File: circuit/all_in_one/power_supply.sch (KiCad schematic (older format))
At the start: 23 parts, among them Q1 2SB647, Q2 2SK2611, U1 LM7805, U2 MC34063A

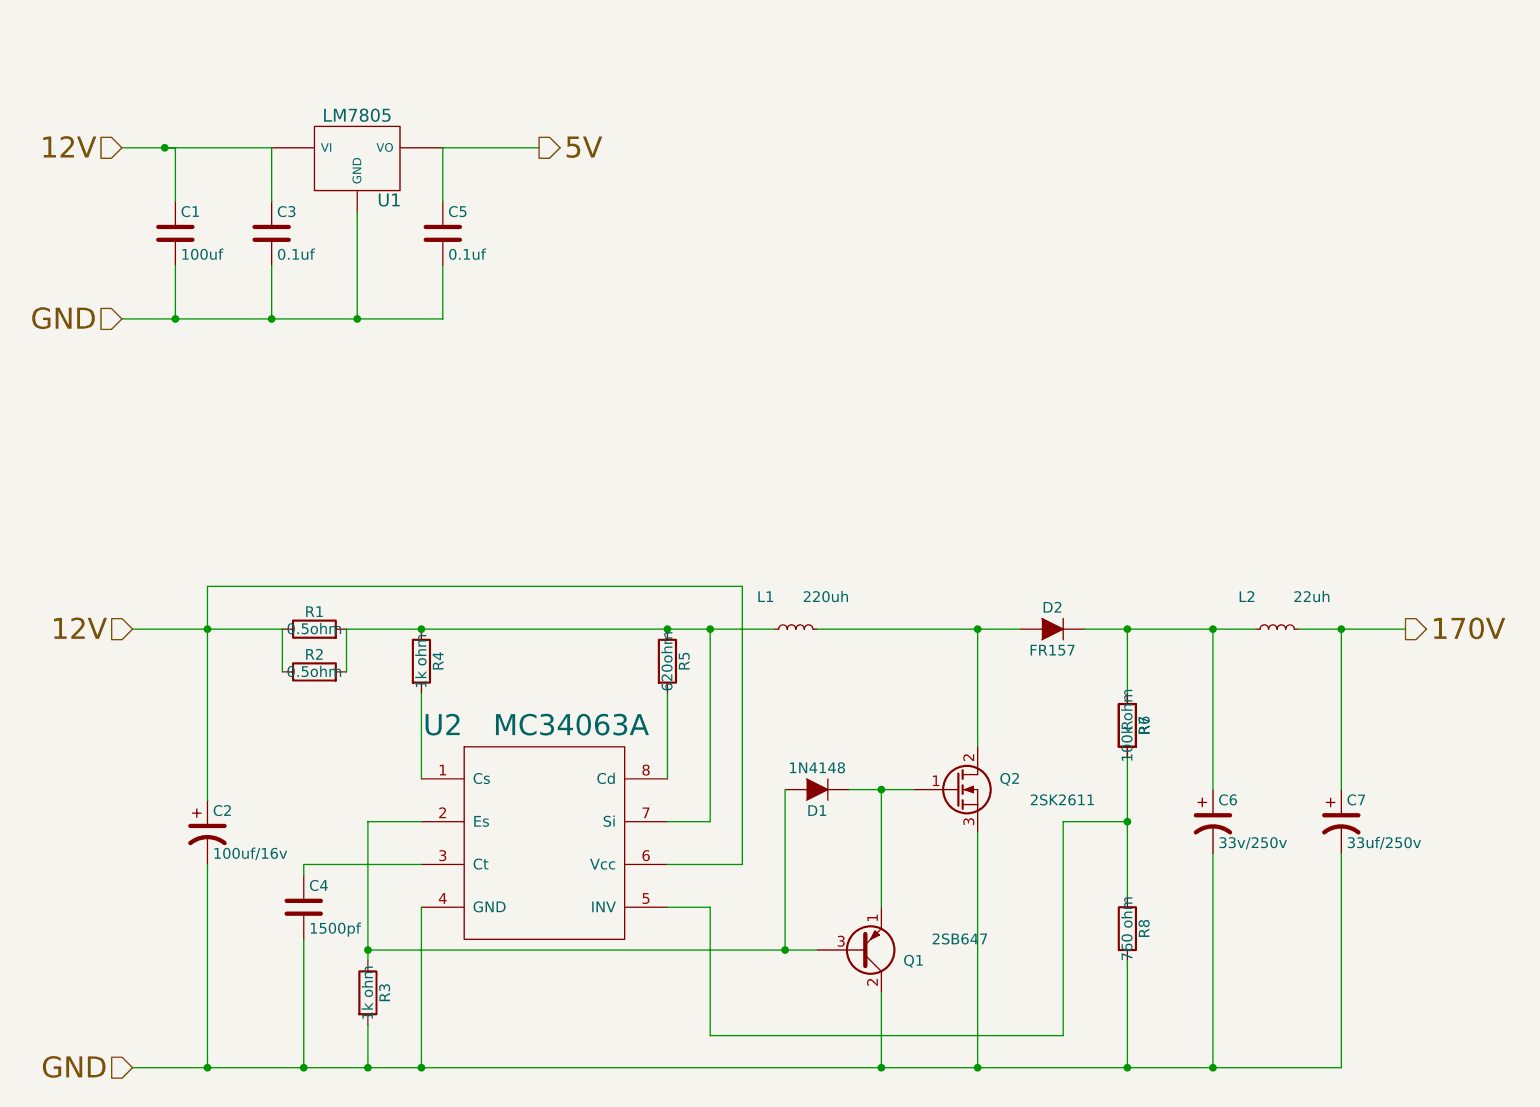
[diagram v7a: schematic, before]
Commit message: Finsihed placing all the components
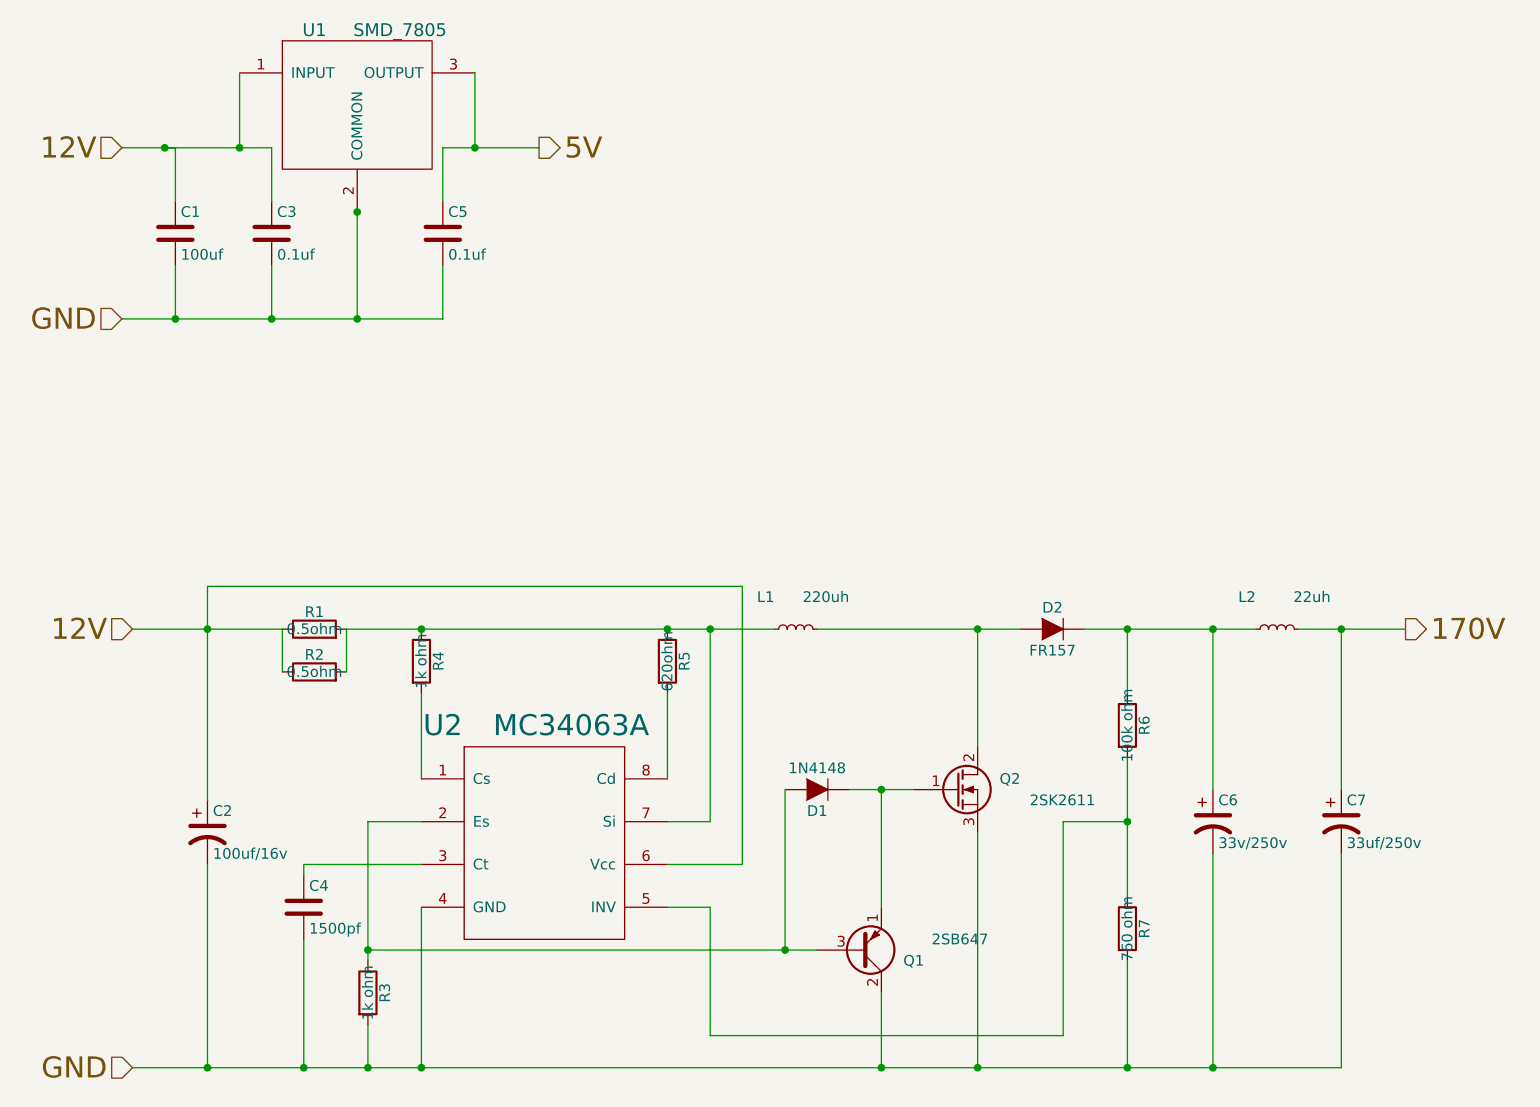
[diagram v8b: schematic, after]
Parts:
- removed R7: R, Resistors_SMD:R_0805_HandSoldering, symbol R
- removed U1: LM7805, Transistors_SMD:sot404, symbol LM7805
- added U1: SMD_7805, TO_SOT_Packages_SMD:TO-252-2Lead, symbol SMD_7805
- Q2: footprint TO_SOT_Packages_THT:TO-220_Neutral123_PadsOnly -> TO_SOT_Packages_THT:TO-247_Vertical_Neutral123
- renumbered R8 to R7
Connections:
- net 12V: now also U1.1 (INPUT)
- net 5V: now also U1.3 (OUTPUT)
- net GND: now also U1.2 (COMMON)
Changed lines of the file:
@@
 $Descr A4 11693 8268
 encoding utf-8
-Sheet 2 6
+Sheet 2 5
 Title ""
 Date ""
@@
 Text HLabel 8500 3950 2    98   Output ~ 0
 170V
-Text HLabel 4450 1700 2    98   Output ~ 0
-5V
-Text HLabel 2500 1700 0    98   Input ~ 0
-12V
-Text HLabel 2500 2500 0    98   Input ~ 0
-GND
-$Comp
-L LM7805 U1
-U 1 1 56462C05
-P 3600 1750
-F 0 "U1" H 3750 1554 60  0000 C CNN
-F 1 "LM7805" H 3600 1950 60  0000 C CNN
-F 2 "Transistors_SMD:sot404" H 3600 1750 60  0001 C CNN
-F 3 "" H 3600 1750 60  0000 C CNN
-	1    3600 1750
-	1    0    0    -1
-$EndComp
 $Comp
 L C C1
@@
 	1    0    0    -1
 $EndComp
-Wire Wire Line
-	3200 2500 3200 2250
-Wire Wire Line
-	2500 2500 4000 2500
-Wire Wire Line
-	4000 2500 4000 2250
-Wire Wire Line
-	4000 1950 4000 1700
-Wire Wire Line
-	3200 1700 3200 1950
-Wire Wire Line
-	3600 2000 3600 2500
-Connection ~ 3600 2500
-Wire Wire Line
-	4000 1700 4450 1700
-Wire Wire Line
-	2500 1700 3200 1700
-Connection ~ 3200 2500
-Wire Wire Line
-	2750 2250 2750 2500
-Connection ~ 2750 2500
-Wire Wire Line
-	2750 1950 2750 1700
-Wire Wire Line
-	2750 1700 2700 1700
-Connection ~ 2700 1700
 $Comp
 L MC34063A U2
@@
 $EndComp
 $Comp
-L R R8
+L R R7
 U 1 1 56463951
 P 7200 5350
-F 0 "R8" V 7280 5350 50  0000 C CNN
+F 0 "R7" V 7280 5350 50  0000 C CNN
 F 1 "760 ohm" V 7200 5350 50  0000 C CNN
 F 2 "Resistors_SMD:R_0805_HandSoldering" V 7130 5350 30  0001 C CNN
@@
 	-1   0    0    1
 $EndComp
-Wire Wire Line
-	3550 3950 5550 3950
-Wire Wire Line
-	3550 3950 3550 4150
-Wire Wire Line
-	3250 3950 3250 4150
-Wire Wire Line
-	3900 4250 3900 4650
-Connection ~ 3900 3950
-Wire Wire Line
-	5050 4250 5050 4650
-Wire Wire Line
-	5250 3950 5250 4850
-Wire Wire Line
-	5250 4850 5050 4850
-Connection ~ 5050 3950
-Wire Wire Line
-	5050 5050 5400 5050
-Wire Wire Line
-	5400 5050 5400 3750
-Wire Wire Line
-	5400 3750 2900 3750
-Wire Wire Line
-	2900 3750 2900 4750
-Text HLabel 2550 3950 0    98   Input ~ 0
-12V
-Text HLabel 2550 6000 0    98   Input ~ 0
-GND
-Wire Wire Line
-	2550 3950 3250 3950
-Connection ~ 2900 3950
-Wire Wire Line
-	2900 5050 2900 6000
-Connection ~ 2900 6000
-Wire Wire Line
-	2550 6000 8200 6000
-Wire Wire Line
-	3900 5250 3900 6000
 $Comp
 L R R3
@@
 	1    0    0    -1
 $EndComp
-Wire Wire Line
-	3350 5400 3350 6000
-Wire Wire Line
-	3350 5100 3350 5050
-Wire Wire Line
-	3650 4850 3650 5500
-Wire Wire Line
-	3650 4850 3900 4850
-Wire Wire Line
-	3350 5050 3900 5050
 $Comp
 L L_Small L1
@@
 	0    -1   -1   0
 $EndComp
-Connection ~ 5250 3950
 $Comp
 L Q_PNP_ECB Q1
@@
 F 0 "Q2" H 6700 4750 50  0000 R CNN
 F 1 "2SK2611" H 7050 4650 50  0000 R CNN
-F 2 "TO_SOT_Packages_THT:TO-220_Neutral123_PadsOnly" H 6600 4800 29  0001 C CNN
+F 2 "TO_SOT_Packages_THT:TO-247_Vertical_Neutral123" H 6600 4800 29  0001 C CNN
 F 3 "" H 6400 4700 60  0000 C CNN
 	1    6400 4700
 	1    0    0    -1
 $EndComp
+Text HLabel 2550 3950 0    98   Input ~ 0
+12V
+Text HLabel 2500 1700 0    98   Input ~ 0
+12V
+Text HLabel 4450 1700 2    98   Output ~ 0
+5V
+Text HLabel 2550 6000 0    98   Input ~ 0
+GND
+Text HLabel 2500 2500 0    98   Input ~ 0
+GND
+$Comp
+L SMD_7805 U1
+U 1 1 56A86285
+P 3050 1250
+F 0 "U1" H 3400 1350 60  0000 C CNN
+F 1 "SMD_7805" H 3800 1350 60  0000 C CNN
+F 2 "TO_SOT_Packages_SMD:TO-252-2Lead" H 3800 1250 60  0001 C CNN
+F 3 "" H 3800 1250 60  0000 C CNN
+	1    3050 1250
+	1    0    0    -1
+$EndComp
+Wire Wire Line
+	3200 2500 3200 2250
+Wire Wire Line
+	2500 2500 4000 2500
+Wire Wire Line
+	4000 2500 4000 2250
+Wire Wire Line
+	4000 1950 4000 1700
+Wire Wire Line
+	3200 1700 3200 1950
+Wire Wire Line
+	3600 2000 3600 2500
+Connection ~ 3600 2500
+Wire Wire Line
+	4000 1700 4450 1700
+Wire Wire Line
+	2500 1700 3200 1700
+Connection ~ 3200 2500
+Wire Wire Line
+	2750 2250 2750 2500
+Connection ~ 2750 2500
+Wire Wire Line
+	2750 1950 2750 1700
+Wire Wire Line
+	2750 1700 2700 1700
+Connection ~ 2700 1700
+Wire Wire Line
+	3550 3950 5550 3950
+Wire Wire Line
+	3550 3950 3550 4150
+Wire Wire Line
+	3250 3950 3250 4150
+Wire Wire Line
+	3900 4250 3900 4650
+Connection ~ 3900 3950
+Wire Wire Line
+	5050 4250 5050 4650
+Wire Wire Line
+	5250 3950 5250 4850
+Wire Wire Line
+	5250 4850 5050 4850
+Connection ~ 5050 3950
+Wire Wire Line
+	5050 5050 5400 5050
+Wire Wire Line
+	5400 5050 5400 3750
+Wire Wire Line
+	5400 3750 2900 3750
+Wire Wire Line
+	2900 3750 2900 4750
+Wire Wire Line
+	2550 3950 3250 3950
+Connection ~ 2900 3950
+Wire Wire Line
+	2900 5050 2900 6000
+Connection ~ 2900 6000
+Wire Wire Line
+	2550 6000 8200 6000
+Wire Wire Line
+	3900 5250 3900 6000
+Wire Wire Line
+	3350 5400 3350 6000
+Wire Wire Line
+	3350 5100 3350 5050
+Wire Wire Line
+	3650 4850 3650 5500
+Wire Wire Line
+	3650 4850 3900 4850
+Wire Wire Line
+	3350 5050 3900 5050
+Connection ~ 5250 3950
 Wire Wire Line
 	5600 4700 5600 5450
@@
 Connection ~ 7600 6000
 Connection ~ 8200 3950
-$Comp
-L R R7
-U 1 1 56481750
-P 7200 4400
-F 0 "R7" V 7280 4400 50  0000 C CNN
-F 1 "R" V 7200 4400 50  0000 C CNN
-F 2 "Resistors_SMD:R_0805_HandSoldering" V 7130 4400 30  0001 C CNN
-F 3 "" H 7200 4400 30  0000 C CNN
-	1    7200 4400
-	1    0    0    -1
-$EndComp
+Connection ~ 3600 2000
+Wire Wire Line
+	3050 1350 3050 1700
+Connection ~ 3050 1700
+Wire Wire Line
+	4150 1350 4150 1700
+Connection ~ 4150 1700
 $EndSCHEMATC
